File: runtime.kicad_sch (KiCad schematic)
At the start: 3 parts, among them U1 AS5600, U2 XIAO-RP2040-DIP

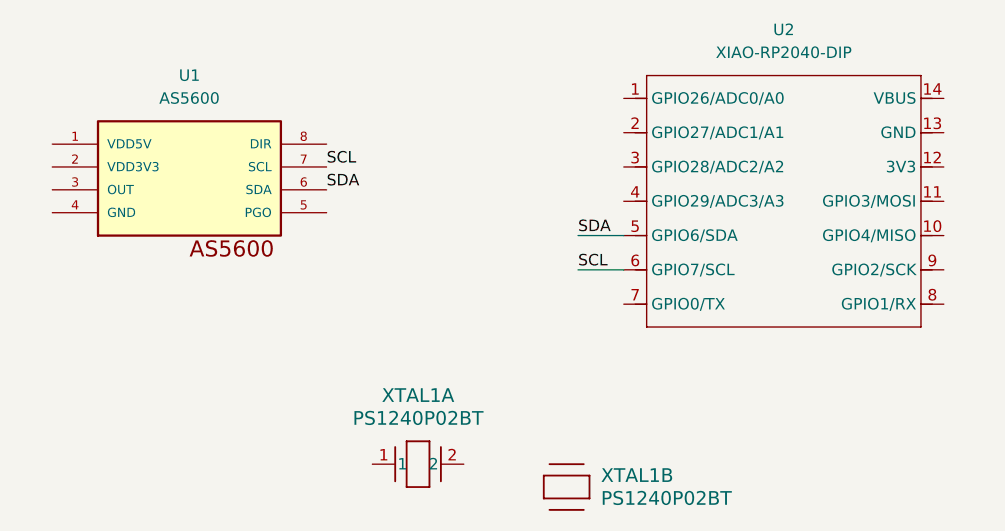
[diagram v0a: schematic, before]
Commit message: fixing up the schematic based on feedback and chatgpt
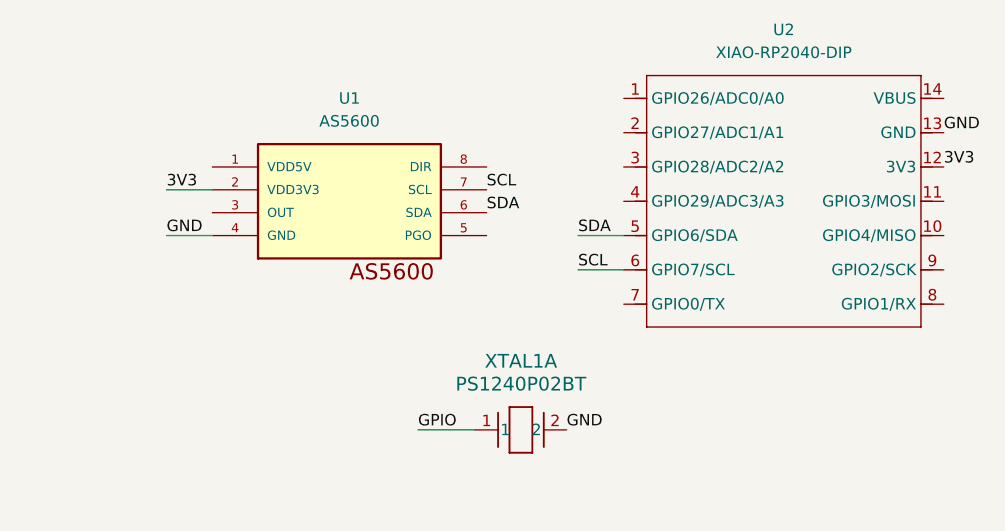
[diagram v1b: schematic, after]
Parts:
- removed unit 2 of XTAL1
- XTAL1: footprint XTAL_PS1240P02BT_TDK -> Buzzer_Beeper:Buzzer_TDK_PS1240P02BT_D12.2mm_H6.5mm
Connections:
- net 3V3: now reaches U1.2 (VDD3V3)
- net 3V3: now also U2.12 (3V3)
- net GND: now reaches U1.4 (GND)
- net GND: now also U2.13 (GND), XTAL1.2
- net GPIO: now reaches XTAL1.1
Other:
- moved on the sheet: U1, XTAL1A
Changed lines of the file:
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@@
+	(wire
+		(pts
+			(xy 113.03 90.17) (xy 118.11 90.17)
+		)
+		(stroke
+			(width 0)
+			(type default)
+		)
+	)
+	(wire
+		(pts
+			(xy 113.03 95.25) (xy 118.11 95.25)
+		)
+		(stroke
+			(width 0)
+			(type default)
+		)
+	)
+	(wire
+		(pts
+			(xy 140.97 116.84) (xy 147.32 116.84)
+		)
+		(stroke
+			(width 0)
+			(type default)
+		)
+	)
 	(wire
 		(pts
@@
 		)
 	)
+	(label "GND"
+		(at 113.03 95.25 0)
+		(effects
+			(font
+				(size 1.27 1.27)
+			)
+			(justify left bottom)
+		)
+	)
+	(label "3V3"
+		(at 113.03 90.17 0)
+		(effects
+			(font
+				(size 1.27 1.27)
+			)
+			(justify left bottom)
+		)
+	)
+	(label "3V3"
+		(at 199.39 87.63 0)
+		(effects
+			(font
+				(size 1.27 1.27)
+			)
+			(justify left bottom)
+		)
+	)
 	(label "SDA"
-		(at 130.81 90.17 0)
+		(at 148.59 92.71 0)
 		(effects
 			(font
@@
 		)
 	)
+	(label "GPIO"
+		(at 140.97 116.84 0)
+		(effects
+			(font
+				(size 1.27 1.27)
+			)
+			(justify left bottom)
+		)
+	)
 	(label "SCL"
-		(at 130.81 87.63 0)
+		(at 148.59 90.17 0)
 		(effects
 			(font
@@
 		)
 	)
-	(symbol
-		(lib_id "2026-07-30_21-14-12:PS1240P02BT")
-		(at 157.48 128.27 0)
-		(unit 2)
-		(body_style 1)
-		(exclude_from_sim no)
-		(in_bom yes)
-		(on_board yes)
-		(in_pos_files yes)
-		(dnp no)
-		(fields_autoplaced yes)
-		(property "Reference" "XTAL1"
-			(at 161.29 121.9199 0)
-			(show_name no)
-			(do_not_autoplace no)
-			(effects
-				(font
-					(size 1.524 1.524)
-				)
-				(justify left)
-			)
-		)
-		(property "Value" "PS1240P02BT"
-			(at 161.29 124.4599 0)
-			(show_name no)
-			(do_not_autoplace no)
-			(effects
-				(font
-					(size 1.524 1.524)
-				)
-				(justify left)
-			)
-		)
-		(property "Footprint" "XTAL_PS1240P02BT_TDK"
-			(at 157.48 128.27 0)
-			(hide yes)
-			(show_name no)
-			(do_not_autoplace no)
-			(effects
-				(font
-					(size 1.27 1.27)
-					(italic yes)
-				)
-			)
-		)
-		(property "Datasheet" "PS1240P02BT"
-			(at 157.48 128.27 0)
-			(hide yes)
-			(show_name no)
-			(do_not_autoplace no)
-			(effects
-				(font
-					(size 1.27 1.27)
-					(italic yes)
-				)
-			)
-		)
-		(property "Description" ""
-			(at 157.48 128.27 0)
-			(hide yes)
-			(show_name no)
-			(do_not_autoplace no)
-			(effects
-				(font
-					(size 1.27 1.27)
-				)
-			)
-		)
-		(pin "1"
-		)
-		(pin "2"
-		)
-		(instances
-			(project "runtime"
-				(path "/d1f4f7e7-9abc-47dc-b707-94eed0ea39e2"
-					(reference "XTAL1")
-					(unit 2)
-				)
-			)
+	(label "GND"
+		(at 157.48 116.84 0)
+		(effects
+			(font
+				(size 1.27 1.27)
+			)
+			(justify left bottom)
+		)
+	)
+	(label "GND"
+		(at 199.39 83.82 0)
+		(effects
+			(font
+				(size 1.27 1.27)
+			)
+			(justify left bottom)
 		)
 	)
 	(symbol
 		(lib_id "AS5600:AS5600")
-		(at 115.57 87.63 0)
+		(at 133.35 90.17 0)
 		(unit 1)
 		(body_style 1)
@@
 		(fields_autoplaced yes)
 		(property "Reference" "U1"
-			(at 115.5774 77.47 0)
+			(at 133.3574 80.01 0)
 			(show_name no)
 			(do_not_autoplace no)
@@
 		)
 		(property "Value" "AS5600"
-			(at 115.5774 80.01 0)
+			(at 133.3574 82.55 0)
 			(show_name no)
 			(do_not_autoplace no)
@@
 		)
 		(property "Footprint" "AS5600:SOIC8"
-			(at 115.57 87.63 0)
+			(at 133.35 90.17 0)
 			(hide yes)
 			(show_name no)
@@
 		)
 		(property "Datasheet" ""
-			(at 115.57 87.63 0)
+			(at 133.35 90.17 0)
 			(hide yes)
 			(show_name no)
@@
 		)
 		(property "Description" "Hall Effect Sensor Rotary Position External Magnet, Not Included Gull Wing"
-			(at 115.57 87.63 0)
+			(at 133.35 90.17 0)
 			(hide yes)
 			(show_name no)
@@
 		)
 		(property "MF" "Ams AG"
-			(at 115.57 87.63 0)
+			(at 133.35 90.17 0)
 			(hide yes)
 			(show_name no)
@@
 		)
 		(property "Package" "None"
-			(at 115.57 87.63 0)
+			(at 133.35 90.17 0)
 			(hide yes)
 			(show_name no)
@@
 		)
 		(property "Price" "None"
-			(at 115.57 87.63 0)
+			(at 133.35 90.17 0)
 			(hide yes)
 			(show_name no)
@@
 		)
 		(property "SnapEDA_Link" "https://www.snapeda.com/parts/AS5600/ams/view-part/?ref=snap"
-			(at 115.57 87.63 0)
+			(at 133.35 90.17 0)
 			(hide yes)
 			(show_name no)
@@
 		)
 		(property "MP" "AS5600"
-			(at 115.57 87.63 0)
+			(at 133.35 90.17 0)
 			(hide yes)
 			(show_name no)
@@
 		)
 		(property "Availability" "Not in stock"
-			(at 115.57 87.63 0)
+			(at 133.35 90.17 0)
 			(hide yes)
 			(show_name no)
@@
 		)
 		(property "Check_prices" "https://www.snapeda.com/parts/AS5600/ams/view-part/?ref=eda"
-			(at 115.57 87.63 0)
+			(at 133.35 90.17 0)
 			(hide yes)
 			(show_name no)
@@
 	(symbol
 		(lib_id "2026-07-30_21-14-12:PS1240P02BT")
-		(at 135.89 120.65 0)
+		(at 147.32 116.84 0)
 		(unit 1)
 		(body_style 1)
@@
 		(fields_autoplaced yes)
 		(property "Reference" "XTAL1"
-			(at 140.97 113.03 0)
+			(at 152.4 109.22 0)
 			(show_name no)
 			(do_not_autoplace no)
@@
 		)
 		(property "Value" "PS1240P02BT"
-			(at 140.97 115.57 0)
+			(at 152.4 111.76 0)
 			(show_name no)
 			(do_not_autoplace no)
@@
 			)
 		)
-		(property "Footprint" "XTAL_PS1240P02BT_TDK"
-			(at 135.89 120.65 0)
+		(property "Footprint" "Buzzer_Beeper:Buzzer_TDK_PS1240P02BT_D12.2mm_H6.5mm"
+			(at 147.32 116.84 0)
 			(hide yes)
 			(show_name no)
@@
 		)
 		(property "Datasheet" "PS1240P02BT"
-			(at 135.89 120.65 0)
+			(at 147.32 116.84 0)
 			(hide yes)
 			(show_name no)
@@
 		)
 		(property "Description" ""
-			(at 135.89 120.65 0)
-			(hide yes)
-			(show_name no)
+			(at 147.32 116.84 0)
+			(hide yes)
+			(show_name no)

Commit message: fixed GPIO issue
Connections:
- net GPIO: now also U2.1 (GPIO26/ADC0/A0)
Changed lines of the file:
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@@
+		)
+	)
+	(wire
+		(pts
+			(xy 157.48 80.01) (xy 163.83 80.01)
+		)
+		(stroke
+			(width 0)
+			(type default)
 		)
 	)
@@
 		(effects
 			(font
+				(size 1.27 1.27)
+			)
+			(justify left bottom)
+		)
+	)
+	(label "GPIO"
+		(at 157.48 80.01 0)
+		(effects
+			(font

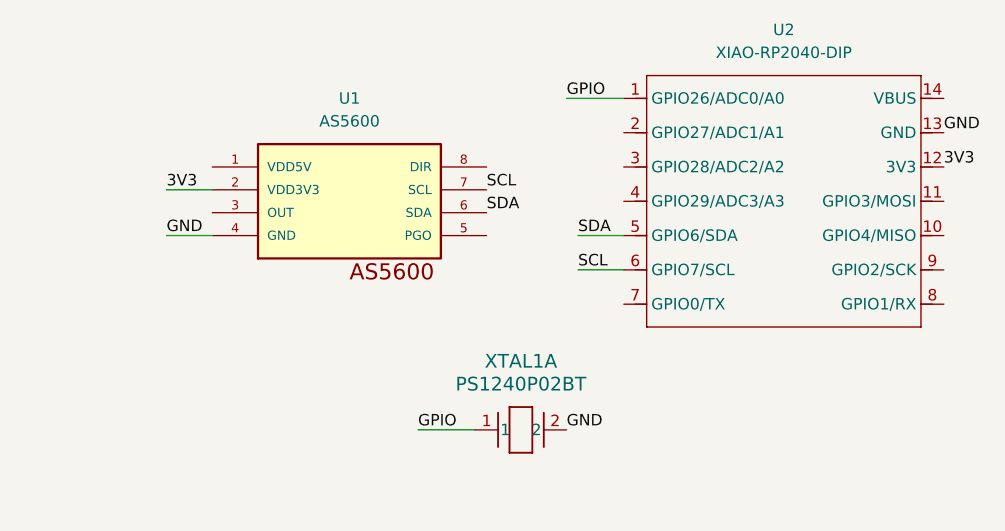
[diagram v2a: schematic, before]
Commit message: finished schematic, worked on pcb
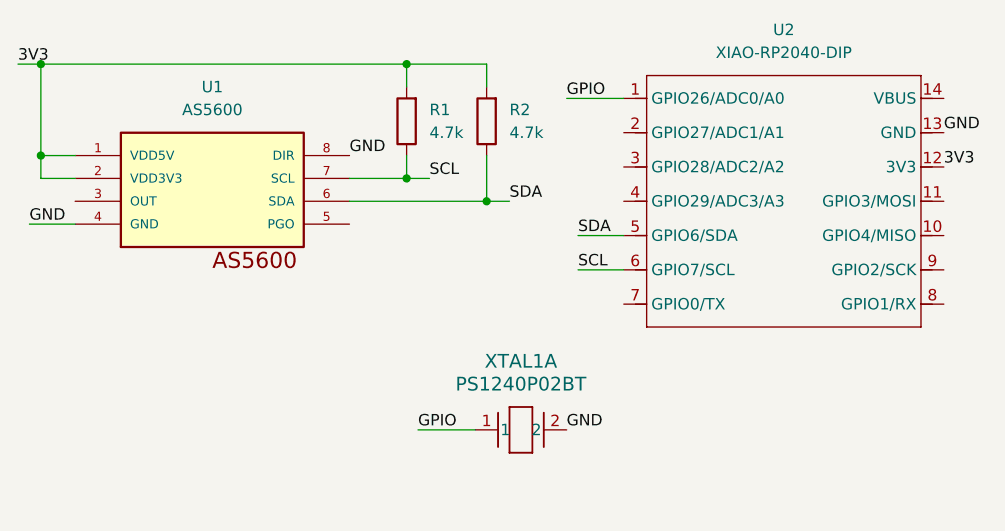
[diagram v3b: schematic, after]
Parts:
- added R1, R2: 4.7k, Resistor_SMD:R_0603_1608Metric, symbol Device:R
- U1: footprint AS5600:SOIC8 -> Package_SO:SOIC-8_3.9x4.9mm_P1.27mm
- U2: footprint Module:MOUDLE14P-XIAO-DIP-SMD -> RF_Module:MCU_Seeed_ESP32C3
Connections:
- net 3V3: now also U1.1 (VDD5V), R1.2, R2.2
- net GND: now also U1.8 (DIR)
- net SCL: now also R1.1
- net SDA: now also R2.1
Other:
- moved on the sheet: U1
